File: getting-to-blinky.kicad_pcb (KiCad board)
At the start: 2 copper layers, 35 x 25 mm, 7 parts, among them U1 ICM7555xB

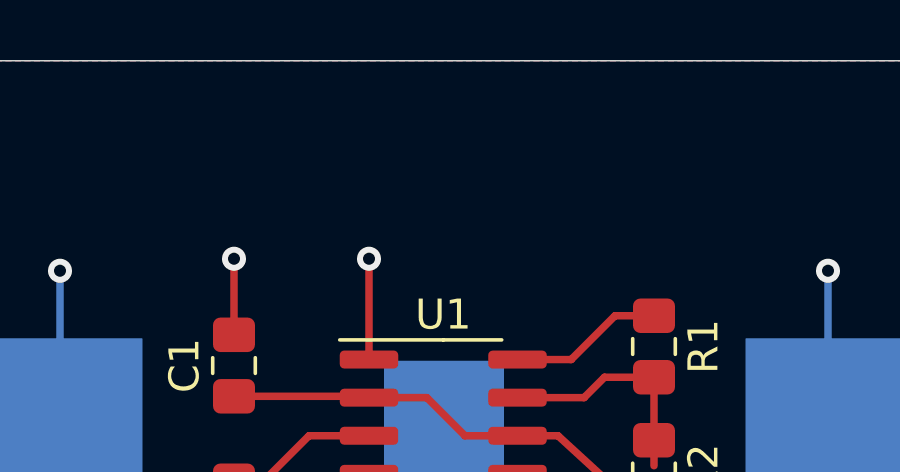
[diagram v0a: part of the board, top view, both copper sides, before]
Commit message: Add title to silkscreen layer.
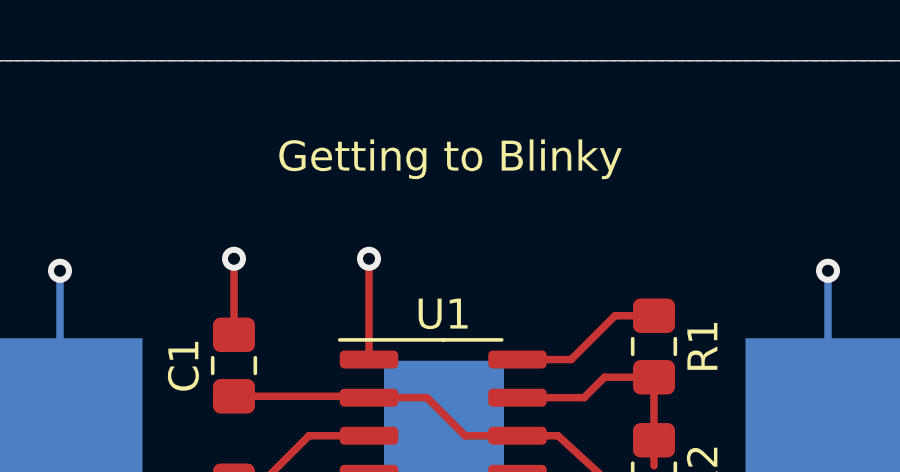
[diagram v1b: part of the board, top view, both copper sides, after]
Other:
- board text added: "Getting to Blinky"
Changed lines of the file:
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@@
   (general
     (thickness 1.6)
-    (drawings 4)
+    (drawings 5)
     (tracks 29)
     (zones 0)
@@
       (net 4 /VDD))
   )
+  (gr_text "Getting to Blinky" (at 137.7 98.2) (layer F.SilkS)
+    (effects (font (size 1 1) (thickness 0.15)))
+  )
   (gr_line (start 120 120) (end 120 95) (layer Edge.Cuts) (width 0.05))
